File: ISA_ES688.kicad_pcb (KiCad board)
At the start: 4 copper layers, 104.1 x 99.1 mm, 114 parts, among them J1 ISA BUS, J2 Interrupt Select, J3 Address Select, J4 DMA Select, J5 Joystick/MIDI, J6 LINE OUT, J7 MIC, J8 LINE IN, J9 SPKR OUT, U1 74LS14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

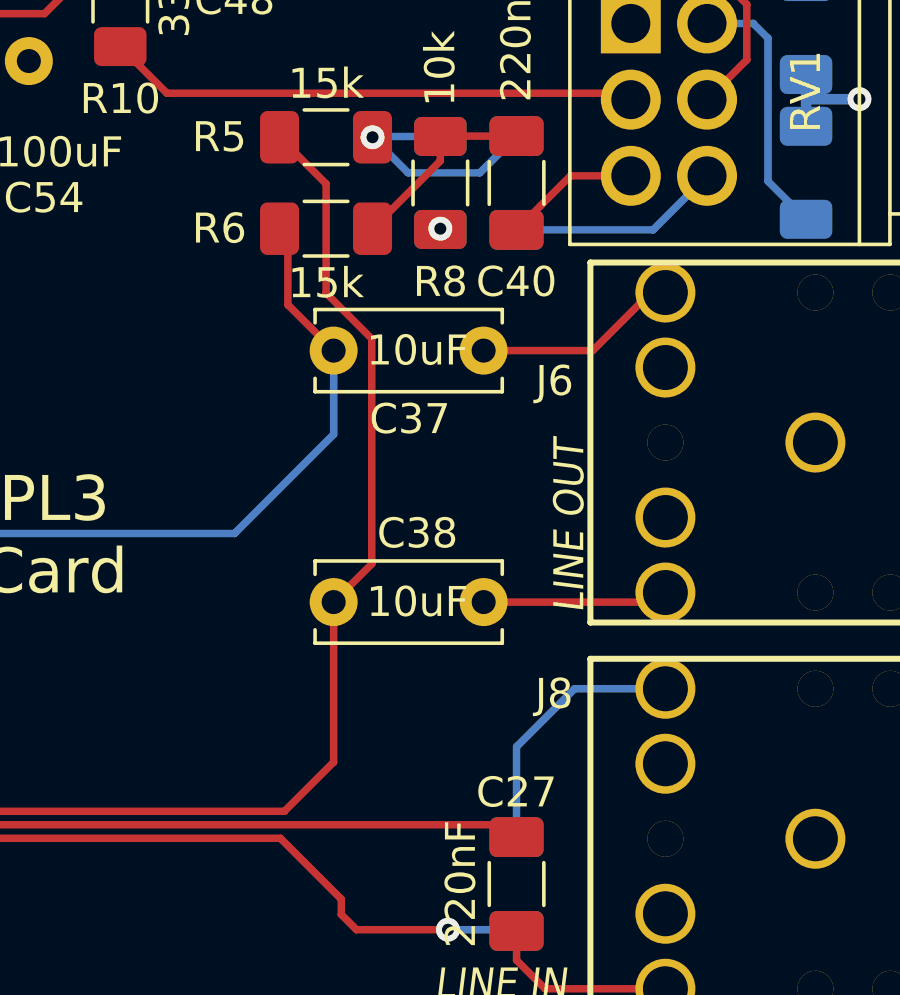
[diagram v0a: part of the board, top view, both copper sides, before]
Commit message: Replaced two ceramics caps with electrolitics
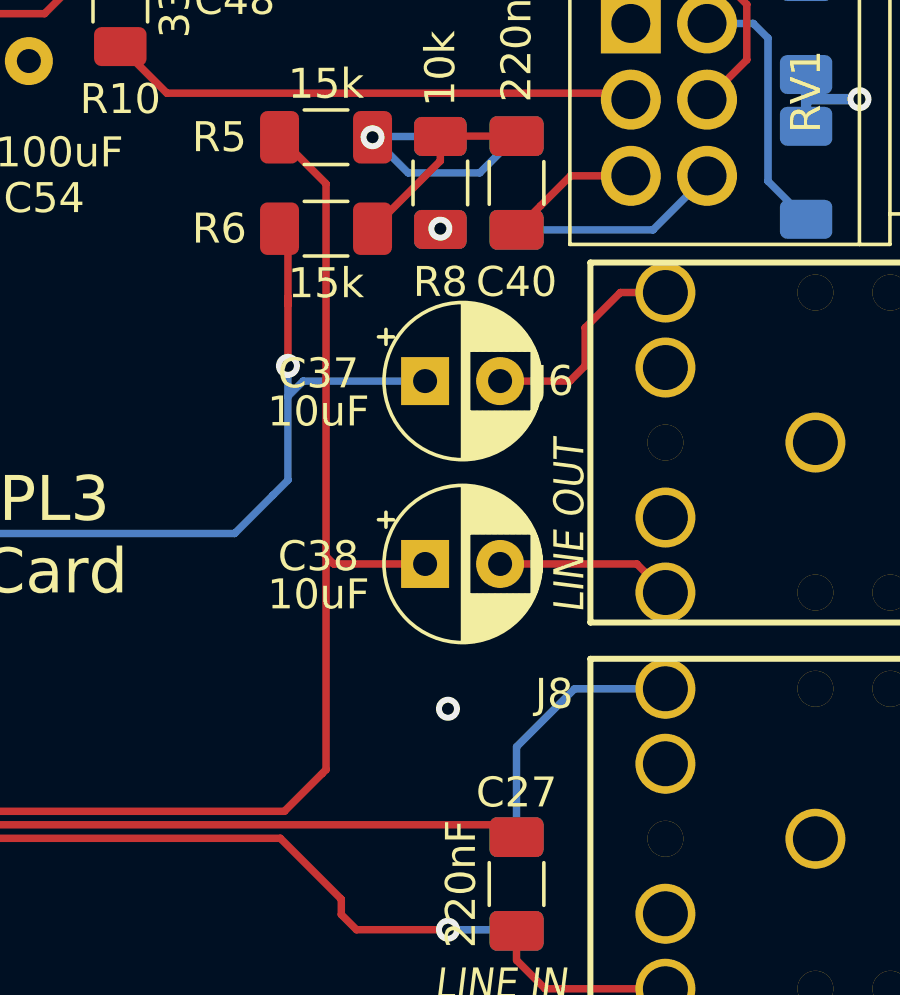
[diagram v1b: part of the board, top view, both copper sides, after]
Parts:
- C37, C38: footprint Capacitor_THT:C_Disc_D6.0mm_W2.5mm_P5.00mm -> Capacitor_THT:CP_Radial_D5.0mm_P2.50mm
- moved C38 3.30 mm to (297.9, 142.2)
- moved C37 3.21 mm to (297.9, 136.1)
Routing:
- net GNDA: track 340.3 -> 375.9 mm, vias 11 -> 12
- net /AOUTL: track 56.4 -> 60.2 mm, vias 1 -> 2
- net /AOUTR: track 72.7 -> 74.9 mm
- net Net-(C37-Pad2): track 6.86 -> 7.96 mm

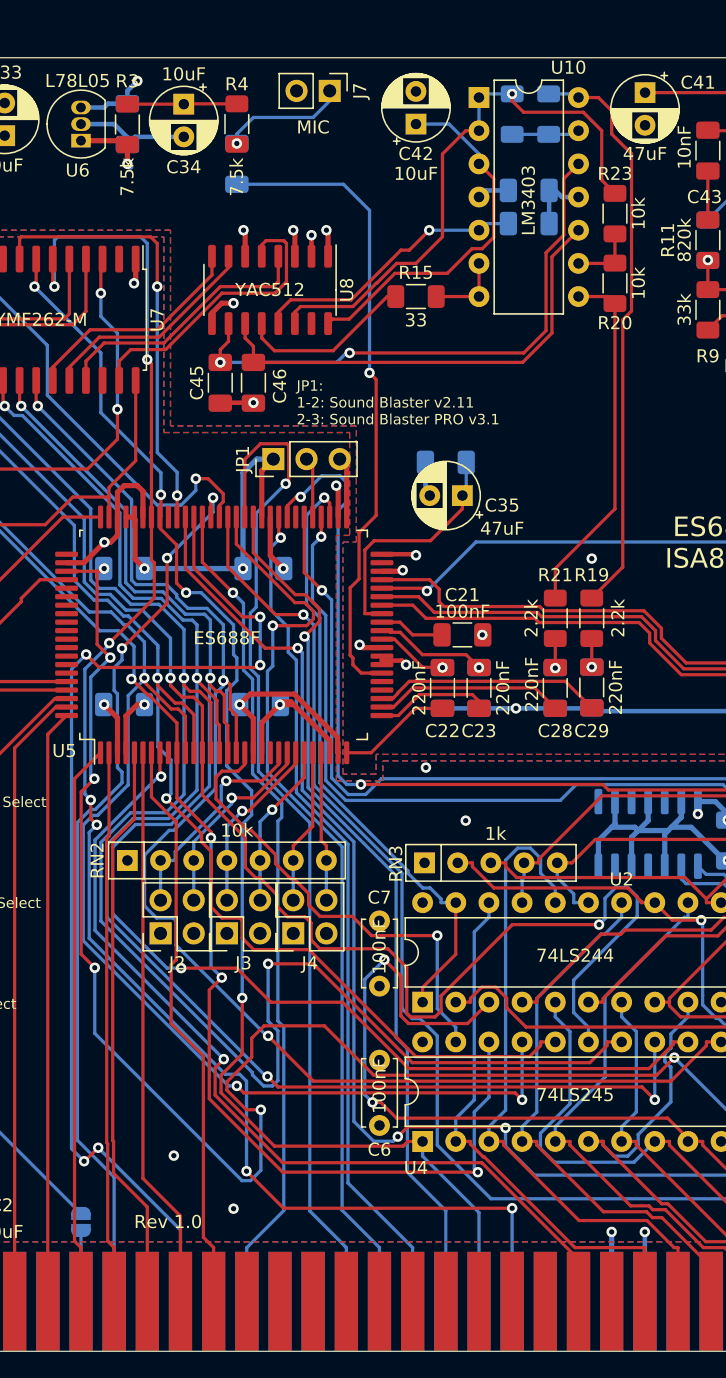
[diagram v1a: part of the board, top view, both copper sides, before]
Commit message: Heavier 12V trace
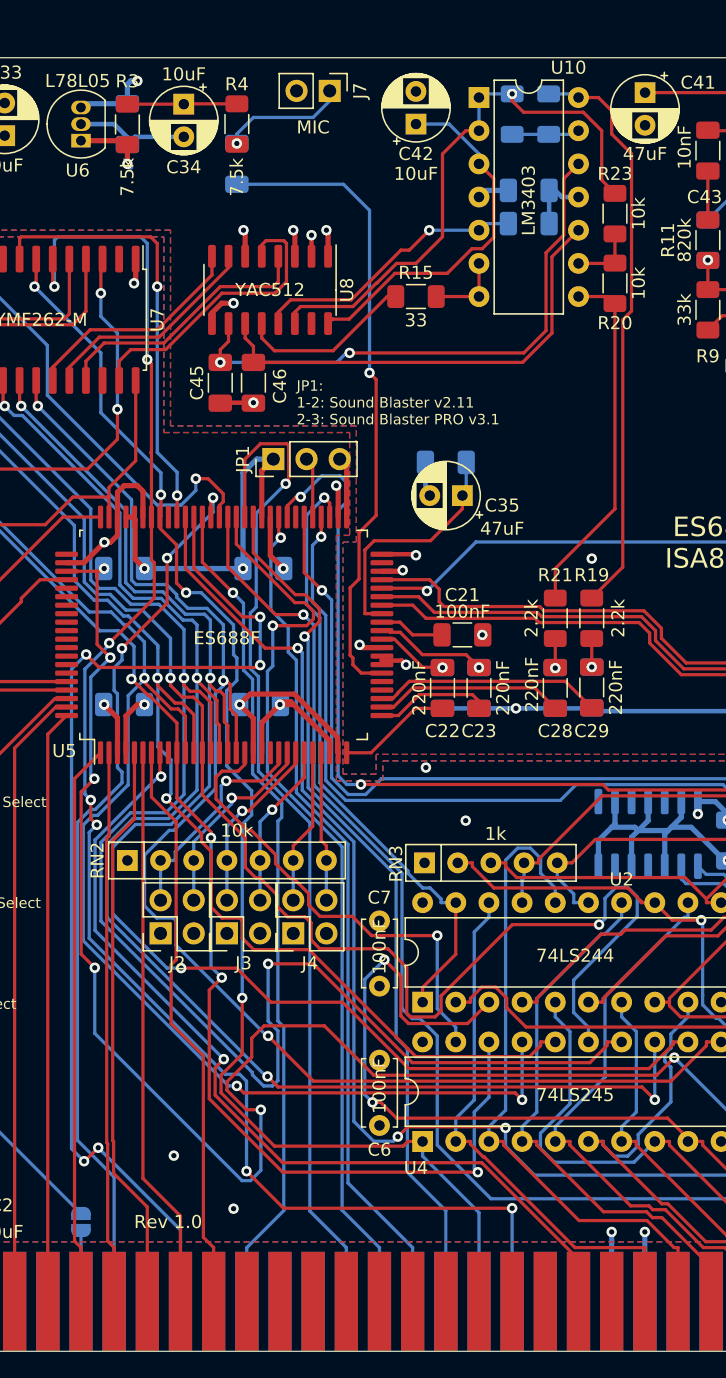
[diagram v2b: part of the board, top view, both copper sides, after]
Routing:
- net +12V: track 147.1 -> 154.2 mm
- net /Filtered_12V: track 28.7 -> 31.5 mm

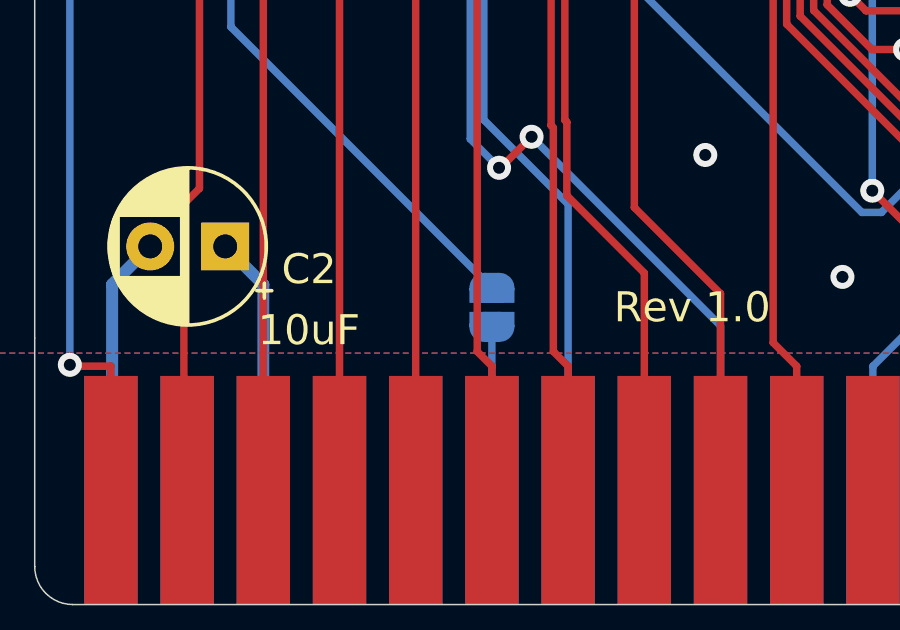
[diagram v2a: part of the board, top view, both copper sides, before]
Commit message: More ground plane!
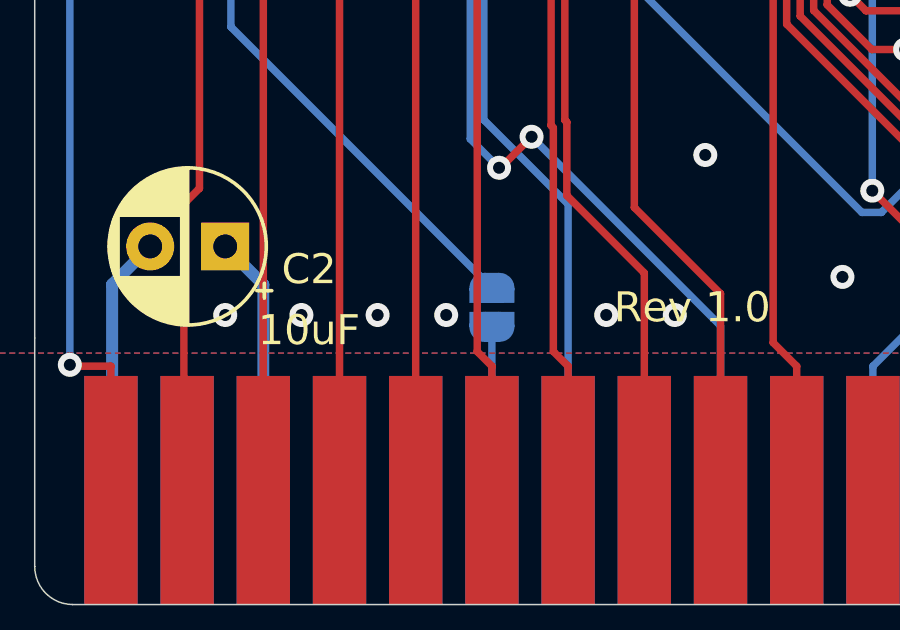
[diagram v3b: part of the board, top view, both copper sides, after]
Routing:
- net GND: track 534.0 -> 552.5 mm, vias 16 -> 22
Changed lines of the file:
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@@
   (general
     (thickness 1.6)
-    (drawings 20)
-    (tracks 2174)
+    (drawings 25)
+    (tracks 2187)
     (zones 0)
     (modules 114)
@@
     )
   )
+  (gr_line (start 310.9468 115.3668) (end 360.6546 115.3668) (layer Dwgs.User) (width 0.15))
+  (gr_line (start 307.34 126.7714) (end 360.7054 126.7714) (layer Dwgs.User) (width 0.15))
+  (gr_line (start 310.9468 138.2014) (end 360.7054 138.2014) (layer Dwgs.User) (width 0.15))
+  (gr_line (start 310.9468 151.384) (end 360.68 151.384) (layer Dwgs.User) (width 0.15))
+  (gr_line (start 315.7728 177.8632) (end 358.14 177.8632) (layer Dwgs.User) (width 0.15))
   (gr_text "Rev 1.0" (at 230.124 193.294) (layer F.SilkS)
     (effects (font (size 1 1) (thickness 0.15)) (justify left))
@@
   (segment (start 309.9432 162.8772) (end 309.9432 193.6112) (width 0.4) (layer In1.Cu) (net 1))
   (segment (start 308.4192 161.3532) (end 309.9432 162.8772) (width 0.4) (layer In1.Cu) (net 1))
+  (via (at 217.17 193.548) (size 0.8) (drill 0.4) (layers F.Cu B.Cu) (net 1))
+  (segment (start 214.884 191.262) (end 217.17 193.548) (width 0.4) (layer In1.Cu) (net 1))
+  (segment (start 214.67 191.262) (end 214.884 191.262) (width 0.4) (layer In1.Cu) (net 1))
+  (segment (start 217.17 193.548) (end 219.71 193.548) (width 0.4) (layer In1.Cu) (net 1))
+  (segment (start 229.87 193.548) (end 232.156 193.548) (width 0.4) (layer In1.Cu) (net 1))
+  (via (at 229.87 193.548) (size 0.8) (drill 0.4) (layers F.Cu B.Cu) (net 1))
+  (via (at 232.156 193.548) (size 0.8) (drill 0.4) (layers F.Cu B.Cu) (net 1))
+  (segment (start 224.536 193.548) (end 229.87 193.548) (width 0.4) (layer In1.Cu) (net 1))
+  (via (at 224.536 193.548) (size 0.8) (drill 0.4) (layers F.Cu B.Cu) (net 1))
+  (segment (start 222.25 193.548) (end 224.536 193.548) (width 0.4) (layer In1.Cu) (net 1))
+  (via (at 222.25 193.548) (size 0.8) (drill 0.4) (layers F.Cu B.Cu) (net 1))
+  (segment (start 219.71 193.548) (end 222.25 193.548) (width 0.4) (layer In1.Cu) (net 1))
+  (via (at 219.71 193.548) (size 0.8) (drill 0.4) (layers F.Cu B.Cu) (net 1))
   (segment (start 258.788 114.3) (end 258.7875 114.3) (width 0.35) (layer B.Cu) (net 2) (status 30))
   (segment (start 229.616 107.658) (end 229.616 107.6575) (width 0.35) (layer B.Cu) (net 2) (status 30))

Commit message: Move connectors slightly forward
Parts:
- moved J6 0.50 mm to (316.0, 138.2)
- moved J8 0.50 mm to (316.0, 151.4)
- moved J9 0.50 mm to (316.0, 115.4)
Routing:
- net GNDA: track 375.9 -> 400.6 mm
- net Net-(C51-Pad2): track 6.96 -> 7.46 mm
- net Net-(C50-Pad2): track 7.53 -> 8.03 mm
- net Net-(C38-Pad2): track 6.35 -> 6.85 mm
- net Net-(C27-Pad2): track 6.33 -> 6.83 mm
- net Net-(C26-Pad2): track 8.79 -> 9.29 mm

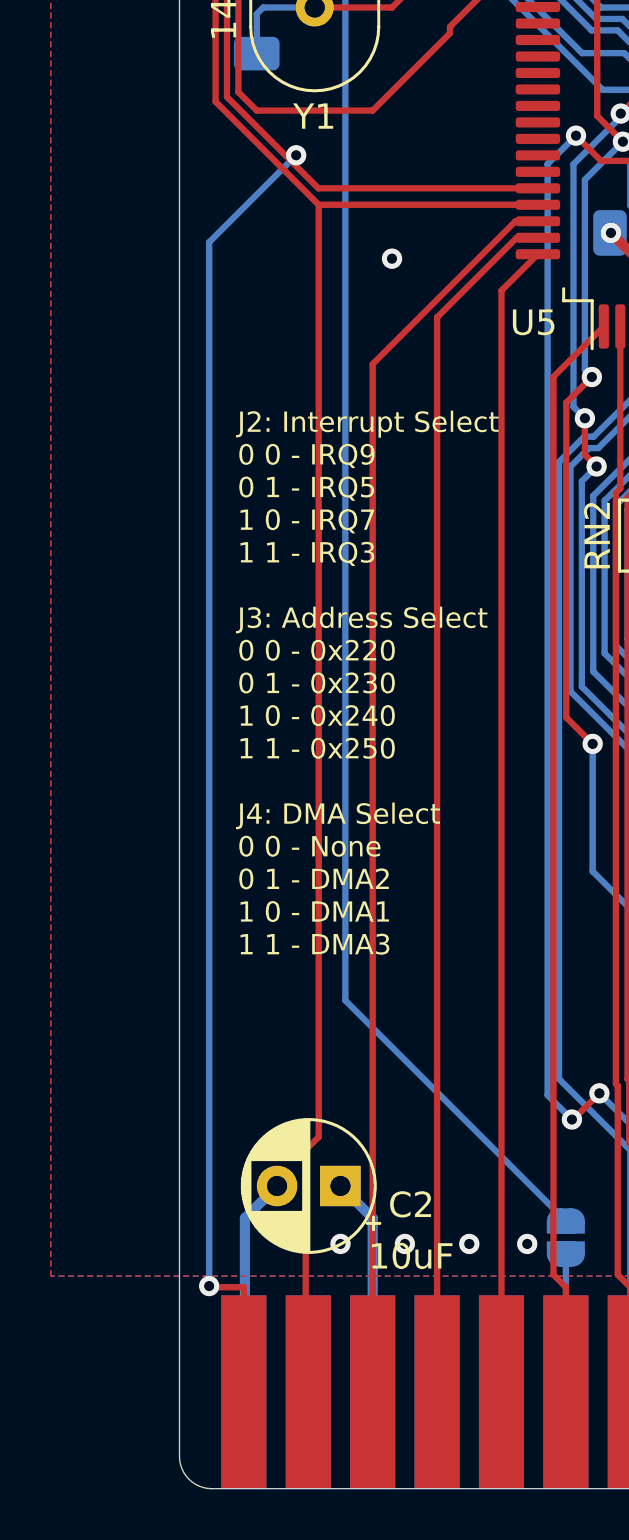
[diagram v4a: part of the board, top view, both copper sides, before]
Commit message: Rerouted some traces
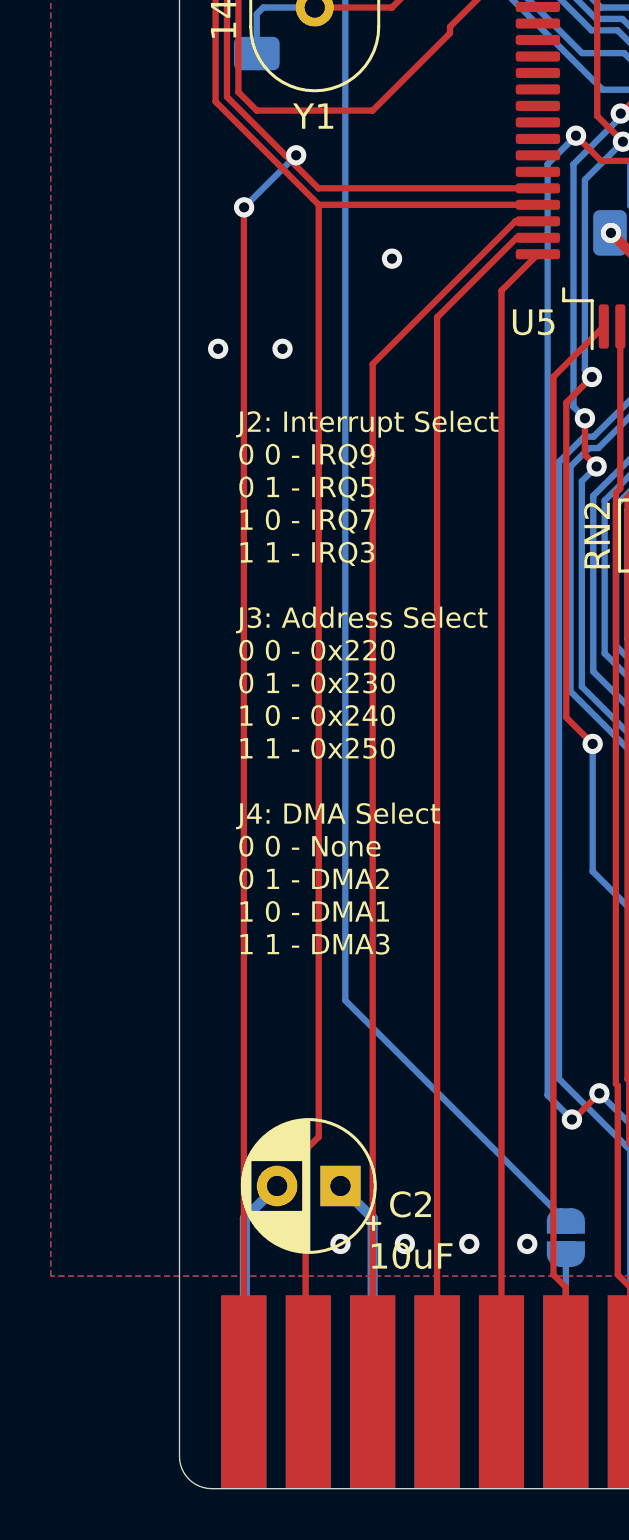
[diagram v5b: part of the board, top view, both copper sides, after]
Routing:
- net GND: track 552.5 -> 560.8 mm, vias 22 -> 24
- net /A0: track 104.6 -> 102.7 mm
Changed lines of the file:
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@@
     (thickness 1.6)
     (drawings 25)
-    (tracks 2194)
+    (tracks 2197)
     (zones 0)
     (modules 114)
@@
   (segment (start 219.71 193.548) (end 222.25 193.548) (width 0.4) (layer In1.Cu) (net 1))
   (via (at 219.71 193.548) (size 0.8) (drill 0.4) (layers F.Cu B.Cu) (net 1))
+  (via (at 212.344 158.242) (size 0.8) (drill 0.4) (layers F.Cu B.Cu) (net 1))
+  (via (at 214.884 158.242) (size 0.8) (drill 0.4) (layers F.Cu B.Cu) (net 1))
+  (segment (start 218.44 154.686) (end 214.884 158.242) (width 0.4) (layer In1.Cu) (net 1))
+  (segment (start 219.202 154.686) (end 218.44 154.686) (width 0.4) (layer In1.Cu) (net 1))
+  (segment (start 212.344 158.242) (end 214.884 158.242) (width 0.4) (layer In1.Cu) (net 1))
   (segment (start 258.788 114.3) (end 258.7875 114.3) (width 0.35) (layer B.Cu) (net 2) (status 30))
   (segment (start 229.616 107.658) (end 229.616 107.6575) (width 0.35) (layer B.Cu) (net 2) (status 30))
@@
   (via (at 291.592 121.666) (size 0.8) (layers F.Cu B.Cu) (net 24) (status 30))
   (segment (start 214.9962 150.6082) (end 215.4222 150.6082) (width 0.25) (layer F.Cu) (net 25))
-  (segment (start 211.9909 195.2086) (end 211.9909 154.0395) (width 0.25) (layer B.Cu) (net 25))
-  (segment (start 211.9909 154.0395) (end 215.4222 150.6082) (width 0.25) (layer B.Cu) (net 25))
-  (segment (start 213.36 195.2547) (end 212.037 195.2547) (width 0.25) (layer F.Cu) (net 25))
-  (segment (start 212.037 195.2547) (end 211.9909 195.2086) (width 0.25) (layer F.Cu) (net 25))
-  (segment (start 213.36 199.39) (end 213.36 195.2547) (width 0.25) (layer F.Cu) (net 25) (status 10))
   (segment (start 214.9962 150.6082) (end 216.299 151.911) (width 0.25) (layer F.Cu) (net 25))
   (segment (start 216.299 151.911) (end 224.957 151.911) (width 0.25) (layer F.Cu) (net 25) (status 20))
-  (via (at 211.9909 195.2086) (size 0.8) (layers F.Cu B.Cu) (net 25))
   (via (at 215.4222 150.6082) (size 0.8) (layers F.Cu B.Cu) (net 25))
   (segment (start 215.656 133.46559) (end 212.69299 136.4286) (width 0.25) (layer F.Cu) (net 25))
@@
   (segment (start 214.99579 150.6082) (end 212.69299 148.3054) (width 0.25) (layer F.Cu) (net 25))
   (segment (start 214.9962 150.6082) (end 214.99579 150.6082) (width 0.25) (layer F.Cu) (net 25))
+  (segment (start 213.36 152.6704) (end 213.3682 152.6622) (width 0.25) (layer F.Cu) (net 25))
+  (via (at 213.3682 152.6622) (size 0.8) (drill 0.4) (layers F.Cu B.Cu) (net 25))
+  (segment (start 213.3682 152.6622) (end 215.4222 150.6082) (width 0.25) (layer B.Cu) (net 25))
+  (segment (start 213.36 199.39) (end 213.36 152.6704) (width 0.25) (layer F.Cu) (net 25))
   (segment (start 216.0785 152.3275) (end 216.312 152.561) (width 0.25) (layer F.Cu) (net 26))
   (segment (start 216.312 152.561) (end 224.957 152.561) (width 0.25) (layer F.Cu) (net 26) (status 20))
